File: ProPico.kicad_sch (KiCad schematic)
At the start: 55 parts, among them J1 USB_C_Receptacle_USB2.0, J2 SWD, J3 LEFT, J4 RIGHT, SW1 BOOTSEL, SW2 RES, U1 FM24CL16B, U2 W25Q16JVUXIQ, U3 AMS1117-3.3, U4 LM4040DBZ-3, U5 RP2040, Y1 ECS-120-12-36-AGN-TR3

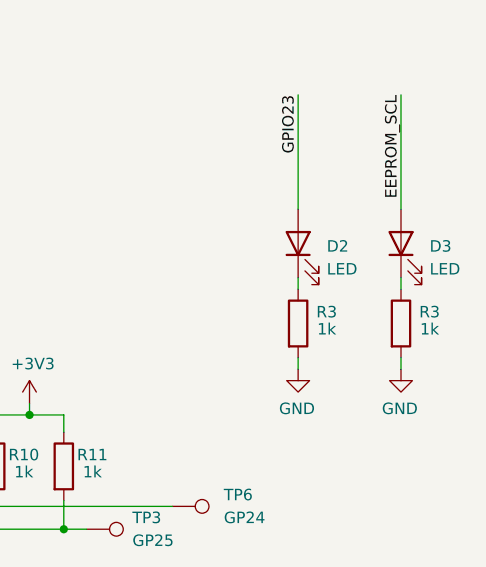
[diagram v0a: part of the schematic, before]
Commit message: Update to kicad 8
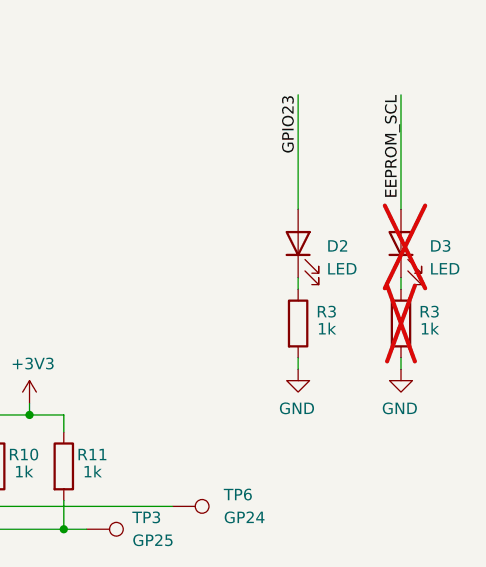
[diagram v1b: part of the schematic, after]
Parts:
- D3, R3: now not fitted

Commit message: Updates to get clean BOM output from fabrication toolkit
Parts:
- J2, J3, J4, JP1, JP2, TP1, TP2, TP3, TP4, TP5, TP6, TP7: now left out of the parts list
- R3: LCSC (none) -> C25543
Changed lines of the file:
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@@
 		(unit 1)
 		(exclude_from_sim no)
-		(in_bom yes)
+		(in_bom no)
 		(on_board yes)
 		(dnp no)
@@
 		(unit 1)
 		(exclude_from_sim no)
-		(in_bom yes)
+		(in_bom no)
 		(on_board yes)
 		(dnp no)
@@
 		(unit 1)
 		(exclude_from_sim no)
-		(in_bom yes)
+		(in_bom no)
 		(on_board yes)
 		(dnp no)
@@
 		(unit 1)
 		(exclude_from_sim no)
-		(in_bom yes)
+		(in_bom no)
 		(on_board yes)
 		(dnp no)
@@
 		(unit 1)
 		(exclude_from_sim no)
-		(in_bom yes)
+		(in_bom no)
 		(on_board yes)
 		(dnp no)
@@
 		(unit 1)
 		(exclude_from_sim no)
-		(in_bom yes)
+		(in_bom no)
 		(on_board yes)
 		(dnp no)
@@
 			)
 		)
+		(property "LCSC" "C25543"
+			(at 138.43 146.05 90)
+			(effects
+				(font
+					(size 1.27 1.27)
+				)
+				(hide yes)
+			)
+		)
 		(pin "1"
 		)
@@
 		(unit 1)
 		(exclude_from_sim no)
-		(in_bom yes)
+		(in_bom no)
 		(on_board yes)
 		(dnp no)
@@
 		(unit 1)
 		(exclude_from_sim no)
-		(in_bom yes)
+		(in_bom no)
 		(on_board yes)
 		(dnp no)
@@
 		(unit 1)
 		(exclude_from_sim no)
-		(in_bom yes)
+		(in_bom no)
 		(on_board yes)
 		(dnp no)
@@
 		(unit 1)
 		(exclude_from_sim no)
-		(in_bom yes)
+		(in_bom no)
 		(on_board yes)
 		(dnp no)
@@
 		(unit 1)
 		(exclude_from_sim no)
-		(in_bom yes)
+		(in_bom no)
 		(on_board yes)
 		(dnp no)
@@
 		(unit 1)
 		(exclude_from_sim no)
-		(in_bom yes)
+		(in_bom no)
 		(on_board yes)
 		(dnp no)

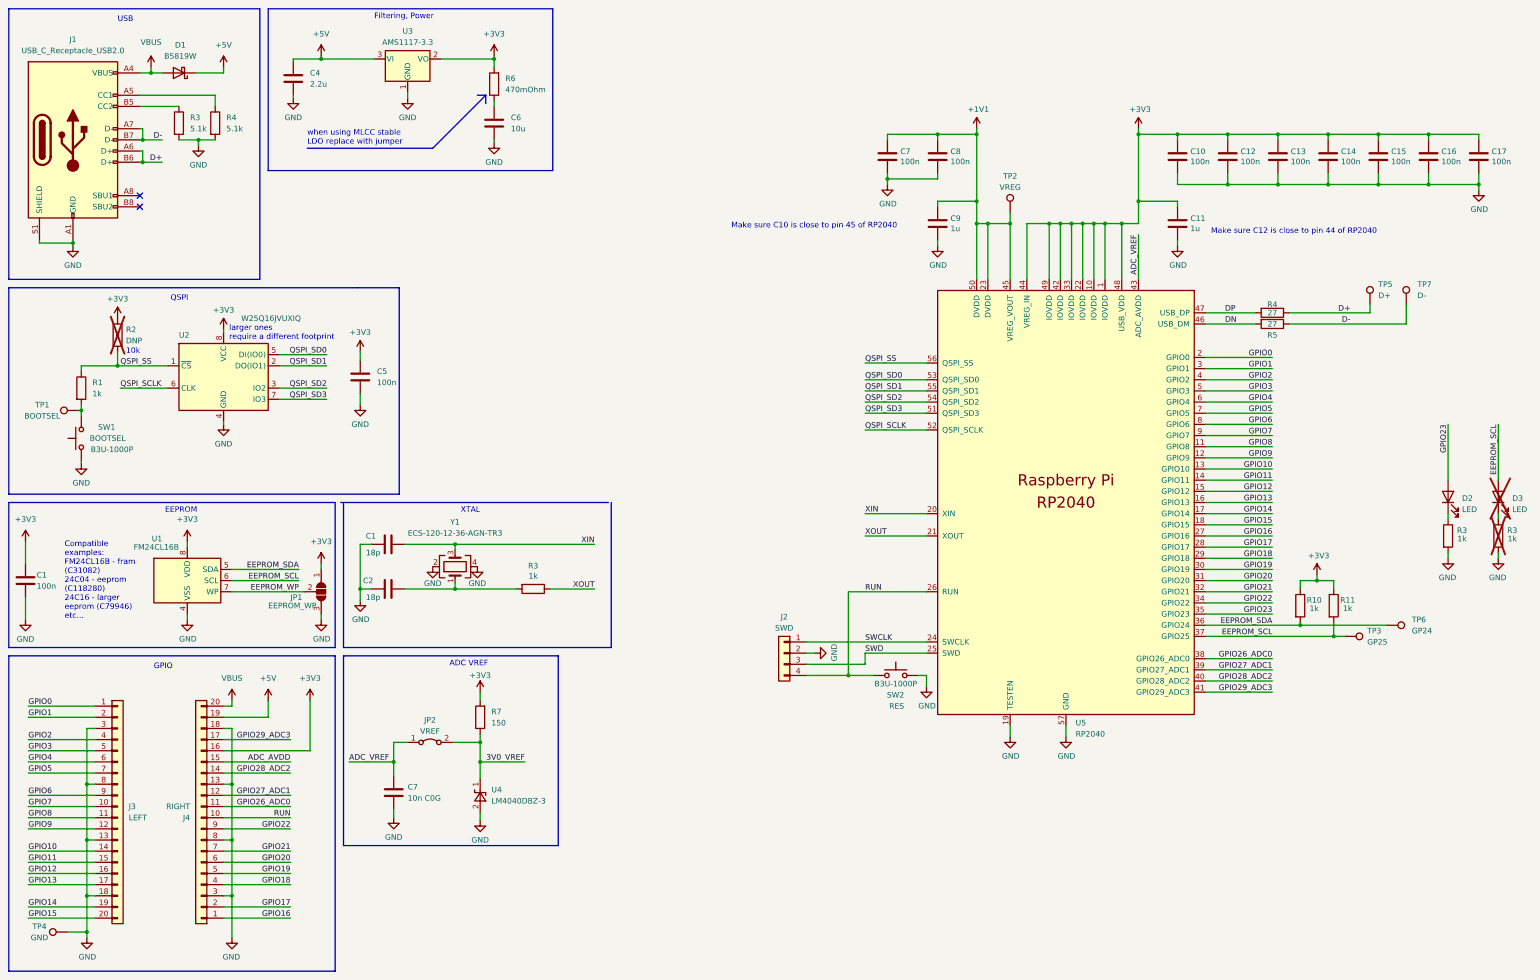
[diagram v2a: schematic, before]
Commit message: Updated LCSC references for cheaper assembly
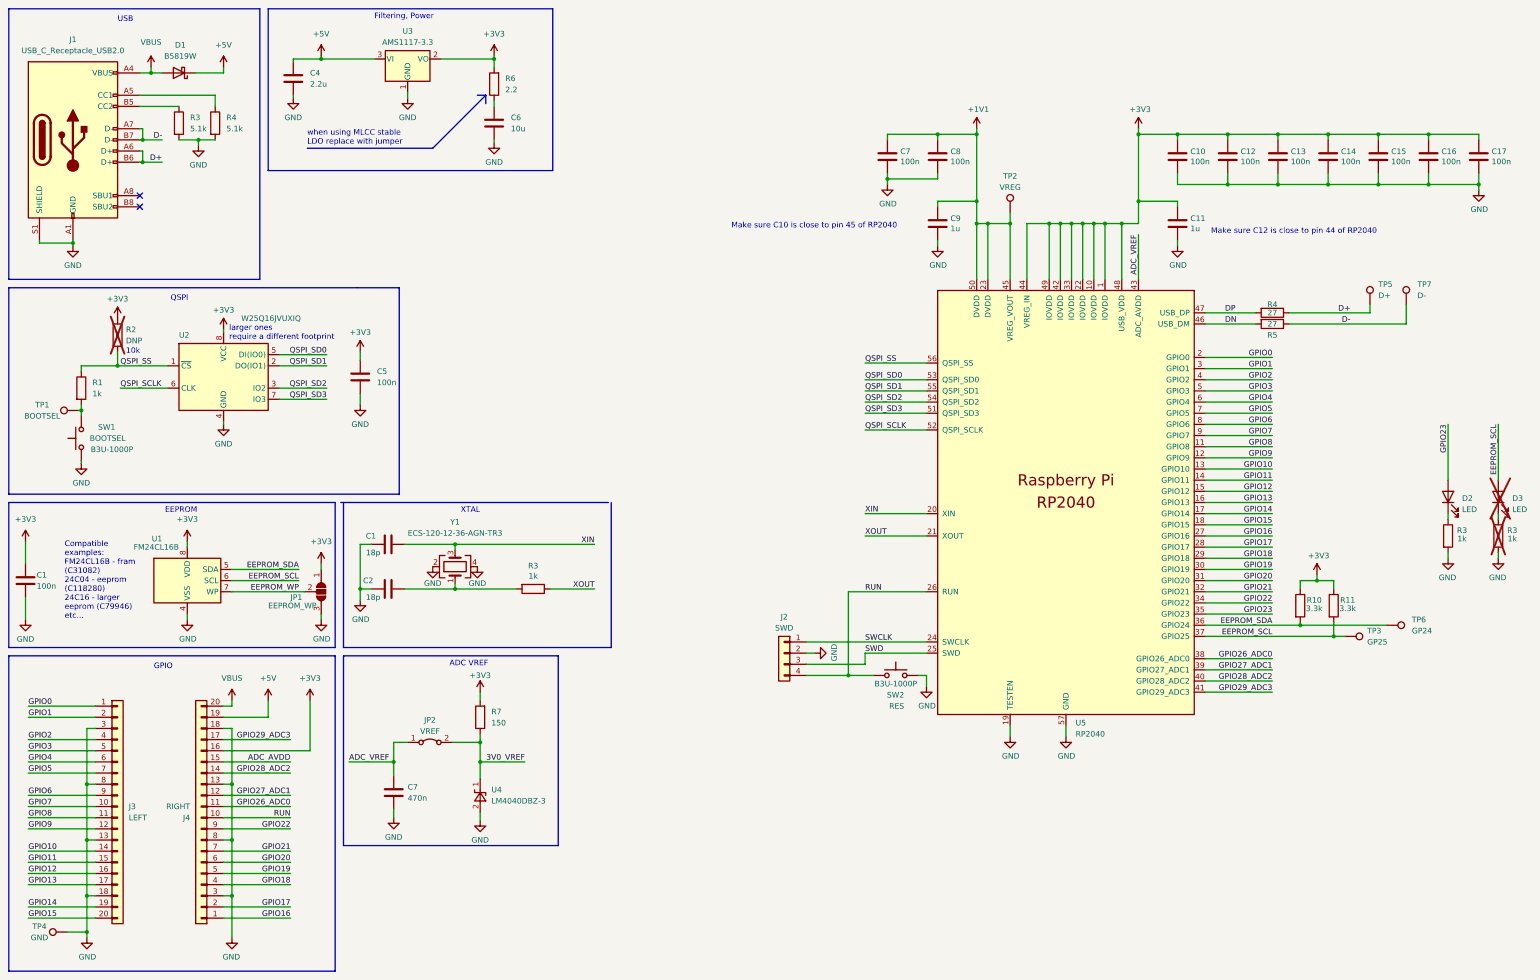
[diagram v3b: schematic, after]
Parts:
- C1, C10, C12, C13, C14, C15, C16, C17, C5, C7, C8: LCSC C77020 -> C1525
- C1, C2: LCSC C126499 -> C1549
- C11, C9: LCSC C77009 -> C52923
- C4: LCSC C57895 -> C23630
- C6: LCSC C162422 -> C15850
- C7: value 10n C0G -> 470n; LCSC C76599 -> C1623
- D1: LCSC C552930 -> C8598
- D2: LCSC C434425 -> C2286
- R1, R3: LCSC C25543 -> C11702
- R10, R11: value 1k -> 3.3k; LCSC C25543 -> C25890
- R3, R4: LCSC C105873 -> C25905
- R6: value 470mOhm -> 2.2; LCSC C2930220 -> C17521
- U3: LCSC C347222 -> C6186
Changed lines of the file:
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@@
 			)
 		)
-		(property "LCSC" "C77020"
+		(property "LCSC" "C1525"
 			(at 330.835 47.625 0)
 			(effects
@@
 			)
 		)
-		(property "LCSC" "C162422"
+		(property "LCSC" "C15850"
 			(at 129.54 40.005 0)
 			(effects
@@
 			)
 		)
-		(property "LCSC" "C77020"
+		(property "LCSC" "C1525"
 			(at 285.115 47.625 0)
 			(effects
@@
 			)
 		)
-		(property "LCSC" "C434425"
+		(property "LCSC" "C2286"
 			(at 346.71 125.095 90)
 			(effects
@@
 			)
 		)
-		(property "LCSC" "C77020"
+		(property "LCSC" "C1525"
 			(at 307.975 47.625 0)
 			(effects
@@
 			)
 		)
-		(property "LCSC" "C77020"
+		(property "LCSC" "C1525"
 			(at 319.405 47.625 0)
 			(effects
@@
 			)
 		)
-		(property "LCSC" "C77009"
+		(property "LCSC" "C52923"
 			(at 230.505 62.865 0)
 			(effects
@@
 			)
 		)
-		(property "LCSC" "C77020"
+		(property "LCSC" "C1525"
 			(at 99.06 97.79 0)
 			(effects
@@
 			)
 		)
-		(property "LCSC" "C552930"
+		(property "LCSC" "C8598"
 			(at 57.785 28.575 0)
 			(effects
@@
 			)
 		)
-		(property "LCSC" "C105873"
+		(property "LCSC" "C25905"
 			(at 66.04 40.005 0)
 			(effects
@@
 			)
 		)
-		(property "Value" "10n C0G"
+		(property "Value" "470n"
 			(at 109.855 193.675 0)
 			(effects
@@
 			)
 		)
-		(property "LCSC" "C76599"
+		(property "LCSC" "C1623"
 			(at 106.68 192.405 0)
 			(effects
@@
 			)
 		)
-		(property "LCSC" "C77020"
+		(property "LCSC" "C1525"
 			(at 219.075 47.625 0)
 			(effects
@@
 			)
 		)
-		(property "LCSC" "C105873"
+		(property "LCSC" "C25905"
 			(at 57.785 40.005 0)
 			(effects
@@
 			)
 		)
-		(property "Value" "470mOhm"
+		(property "Value" "2.2"
 			(at 132.08 32.385 0)
 			(effects
@@
 			)
 		)
-		(property "LCSC" "C2930220"
+		(property "LCSC" "C17521"
 			(at 129.54 31.115 0)
 			(effects
@@
 			)
 		)
-		(property "LCSC" "C25543"
+		(property "LCSC" "C11702"
 			(at 35.56 100.33 0)
 			(effects
@@
 			)
 		)
-		(property "LCSC" "C25543"
+		(property "LCSC" "C11702"
 			(at 138.43 146.05 90)
 			(effects
@@
 			)
 		)
-		(property "LCSC" "C77020"
+		(property "LCSC" "C1525"
 			(at 296.545 47.625 0)
 			(effects
@@
 			)
 		)
-		(property "LCSC" "C77009"
+		(property "LCSC" "C52923"
 			(at 285.115 62.865 0)
 			(effects
@@
 			)
 		)
-		(property "Value" "1k"
+		(property "Value" "3.3k"
 			(at 323.85 150.495 0)
 			(effects
@@
 			)
 		)
-		(property "LCSC" "C25543"
+		(property "LCSC" "C25890"
 			(at 320.675 149.86 0)
 			(effects
@@
 			)
 		)
-		(property "LCSC" "C25543"
+		(property "LCSC" "C11702"
 			(at 346.71 133.985 0)
 			(effects
@@
 			)
 		)
-		(property "LCSC" "C77020"
+		(property "LCSC" "C1525"
 			(at 230.505 47.625 0)
 			(effects
@@
 			)
 		)
-		(property "LCSC" "C57895"
+		(property "LCSC" "C23630"
 			(at 83.82 29.845 0)
 			(effects
@@
 			)
 		)
-		(property "LCSC" "C126499"
+		(property "LCSC" "C1549"
 			(at 105.41 146.05 90)
 			(effects
@@
 			)
 		)
-		(property "LCSC" "C77020"
+		(property "LCSC" "C1525"
 			(at 353.695 47.625 0)
 			(effects
@@
 			)
 		)
-		(property "LCSC" "C77020"
+		(property "LCSC" "C1525"
 			(at 342.265 47.625 0)
 			(effects
@@
 			)
 		)
-		(property "LCSC" "C77020"
+		(property "LCSC" "C1525"
 			(at 22.86 144.145 0)
 			(effects
@@
 			)
 		)
-		(property "LCSC" "C347222"
+		(property "LCSC" "C6186"
 			(at 109.855 25.4 0)
 			(effects
@@
 			)
 		)
-		(property "LCSC" "C126499"
+		(property "LCSC" "C1549"
 			(at 105.41 135.89 90)
 			(effects
@@
 			)
 		)
-		(property "Value" "1k"
+		(property "Value" "3.3k"
 			(at 316.23 150.495 0)
 			(effects
@@
 			)
 		)
-		(property "LCSC" "C25543"
+		(property "LCSC" "C25890"
 			(at 313.055 149.86 0)
 			(effects
